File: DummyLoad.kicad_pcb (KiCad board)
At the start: 2 copper layers, 71 x 37 mm, 30 parts, among them J1 RF In, J2 RF Out, J3 Conn_01x02_Pin

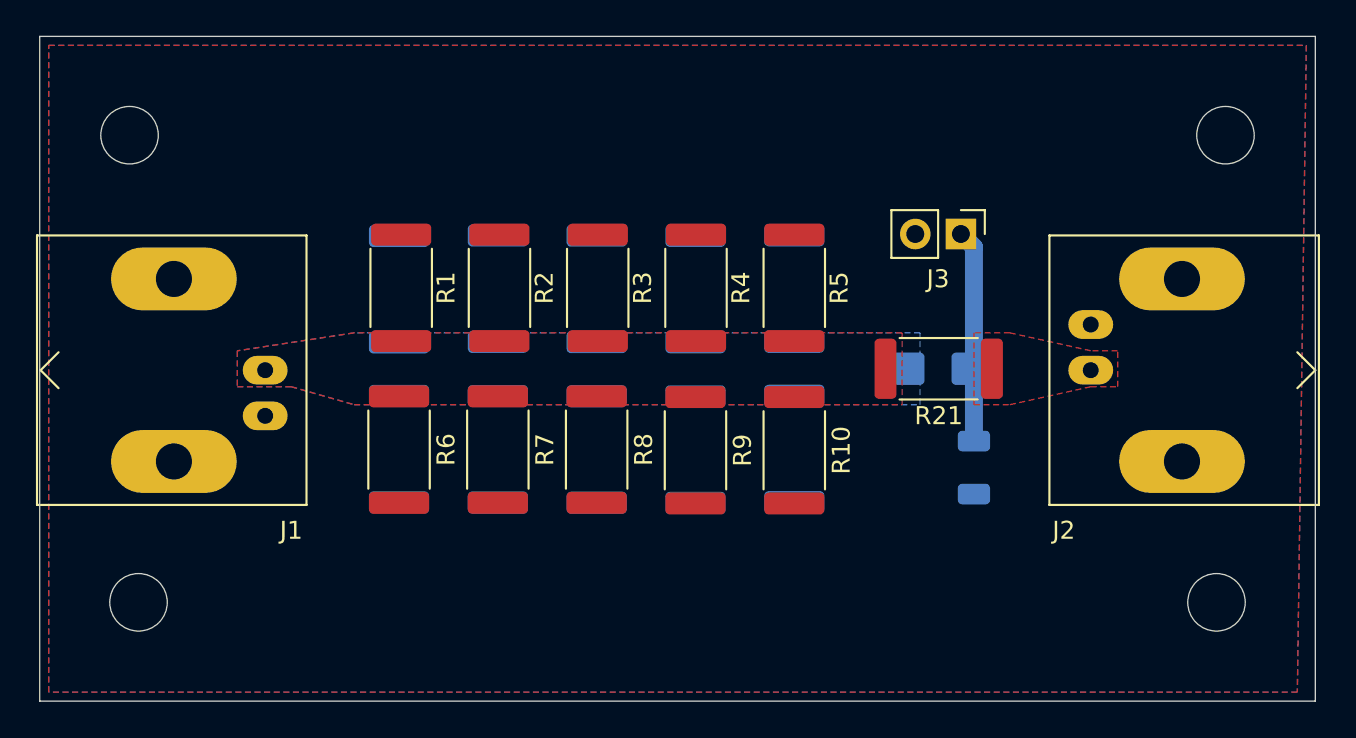
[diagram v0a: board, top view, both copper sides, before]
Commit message: Update PCB footprints, add test points and enable DRC
Enable run_drc in the GitHub workflow and apply extensive footprint changes in DummyLoad.kicad_pcb: add THT test points, convert multiple resistors from 2512 to 1206 footprints (position/size/pad updates and 3D model path changes), update connector metadata (datasheet and Mouser PN), adjust mounting hole/testpoint footprints and silkscreen/pad geometry, and add part metadata (Mouser PNs, datasheet links, zone_connect). These edits correct footprint footprints/metadata and prepare the board for DRC and gerber generation.
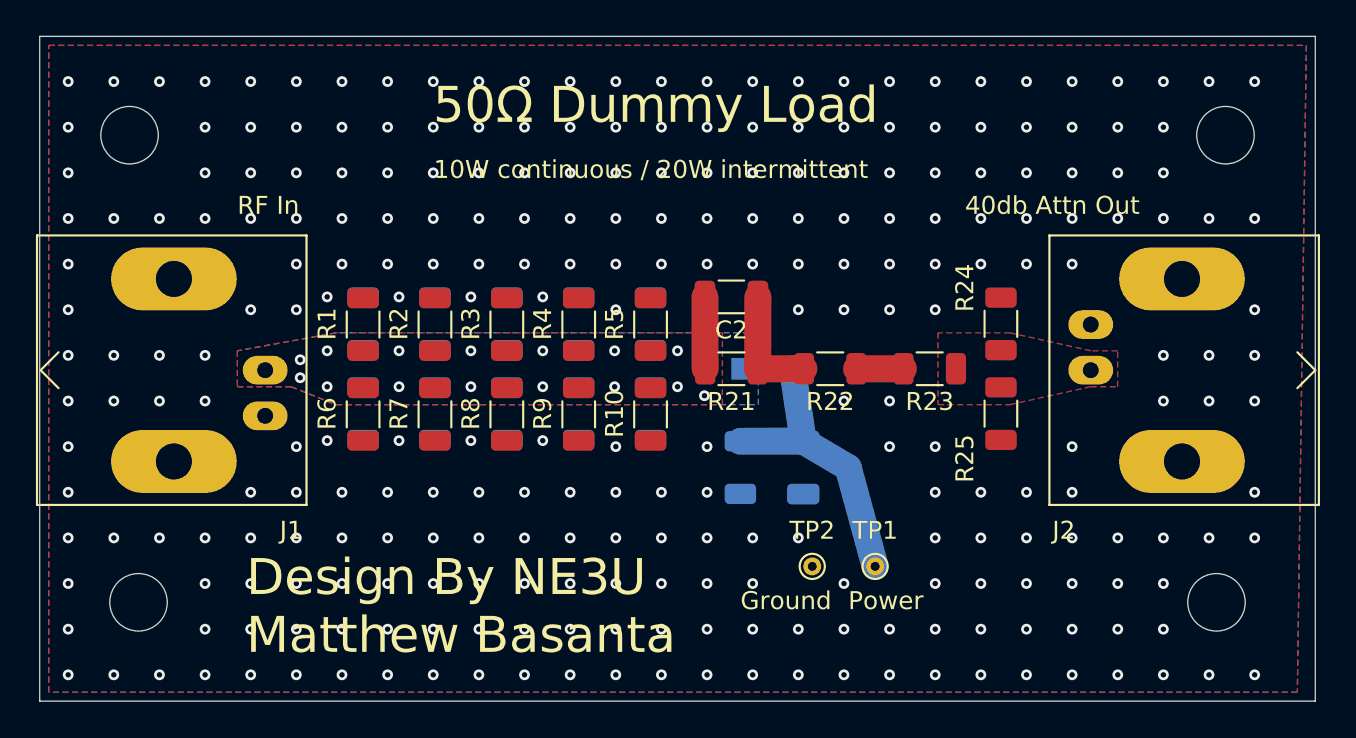
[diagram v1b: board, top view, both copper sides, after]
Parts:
- removed J3: Conn_01x02_Pin, Connector_PinHeader_2.54mm:PinHeader_1x02_P2.54mm_Vertical
- added C2: C, Capacitor_SMD:C_1206_3216Metric, F.Cu at (137.0, 72.0)
- added R22: 820, Resistor_SMD:R_1206_3216Metric, F.Cu at (142.5, 76.0)
- added R23: 820, Resistor_SMD:R_1206_3216Metric, F.Cu at (148.0, 76.0)
- added R24: 102, Resistor_SMD:R_1206_3216Metric, F.Cu at (152.0, 73.5)
- added R25: 102, Resistor_SMD:R_1206_3216Metric, F.Cu at (152.0, 78.5)
- added R26: 100K, Resistor_SMD:R_1206_3216Metric, B.Cu at (137.5, 81.5)
- added TP1: Power Out, TestPoint:TestPoint_THTPad_D1.0mm_Drill0.5mm, F.Cu at (145.0, 87.0)
- added TP2: GND, TestPoint:TestPoint_THTPad_D1.0mm_Drill0.5mm, F.Cu at (141.5, 87.0)
- D1: footprint Diode_SMD:D_SMA -> Diode_SMD:Nexperia_CFP3_SOD-123W
- R1, R10, R11, R12, R13, R14, R15, R16, R17, R18, R19, R2, R20, R3, R4, R5, R6, R7, R8, R9: footprint Resistor_SMD:R_2512_6332Metric -> Resistor_SMD:R_1206_3216Metric
- R21: value 1K -> 820; footprint Resistor_SMD:R_2512_6332Metric -> Resistor_SMD:R_1206_3216Metric
- moved R21 11.5 mm to (137.0, 76.0)
- moved C1 9.50 mm to (141.0, 81.5)
- moved D1 9.50 mm to (139.0, 76.0)
- moved R5 8.26 mm to (132.5, 73.5)
- moved R10 8.25 mm to (132.5, 78.5)
- moved R11 8.24 mm to (132.5, 73.5)
- moved R16 8.24 mm to (132.5, 78.5)
- moved R4 6.84 mm to (128.5, 73.5)
- moved R17 6.80 mm to (128.5, 78.5)
- moved R9 6.80 mm to (128.5, 78.5)
- moved R12 6.78 mm to (128.5, 73.5)
- moved R3 5.45 mm to (124.5, 73.5)
- moved R18 5.38 mm to (124.5, 78.5)
- moved R8 5.37 mm to (124.5, 78.5)
- moved R13 5.36 mm to (124.5, 73.5)
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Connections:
- net PWR renamed Net-(D1-K)
- R21 pad 1: RF_Out -> Net-(C2-Pad1)
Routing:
- net Net-(C2-Pad1): track 0.00 -> 6.58 mm
- net Net-(D1-K): track 11.8 -> 16.2 mm
- net RF_In: track 0.00 -> 4.00 mm, vias 0 -> 15
- net Net-(R22-Pad1): track 0.00 -> 2.61 mm
- net GND: vias 0 -> 272
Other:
- board text added: "10W continuous / 20W intermittent"
- board text added: "40db Attn Out"
- board text added: "50Ω Dummy Load"
- board text added: "Design By NE3U Matthew Basanta"
- board text added: "Ground"
- board text added: "Power"
- board text added: "RF In"

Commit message: Change diode value to 1N5711
Update the diode 'Value' property from 1N4004 to 1N5711 in both the KiCad schematic and PCB files (DummyLoad.kicad_sch and DummyLoad.kicad_pcb) so the schematic and board reflect the new component selection.
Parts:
- D1: value 1N4004 -> 1N5711
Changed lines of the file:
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@@
 			)
 		)
-		(property "Value" "1N4004"
+		(property "Value" "1N5711"
 			(at 0 -2 0)
 			(layer "B.Fab")
